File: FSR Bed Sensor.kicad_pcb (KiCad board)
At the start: 2 copper layers, 25.4 x 25.4 mm, 6 parts

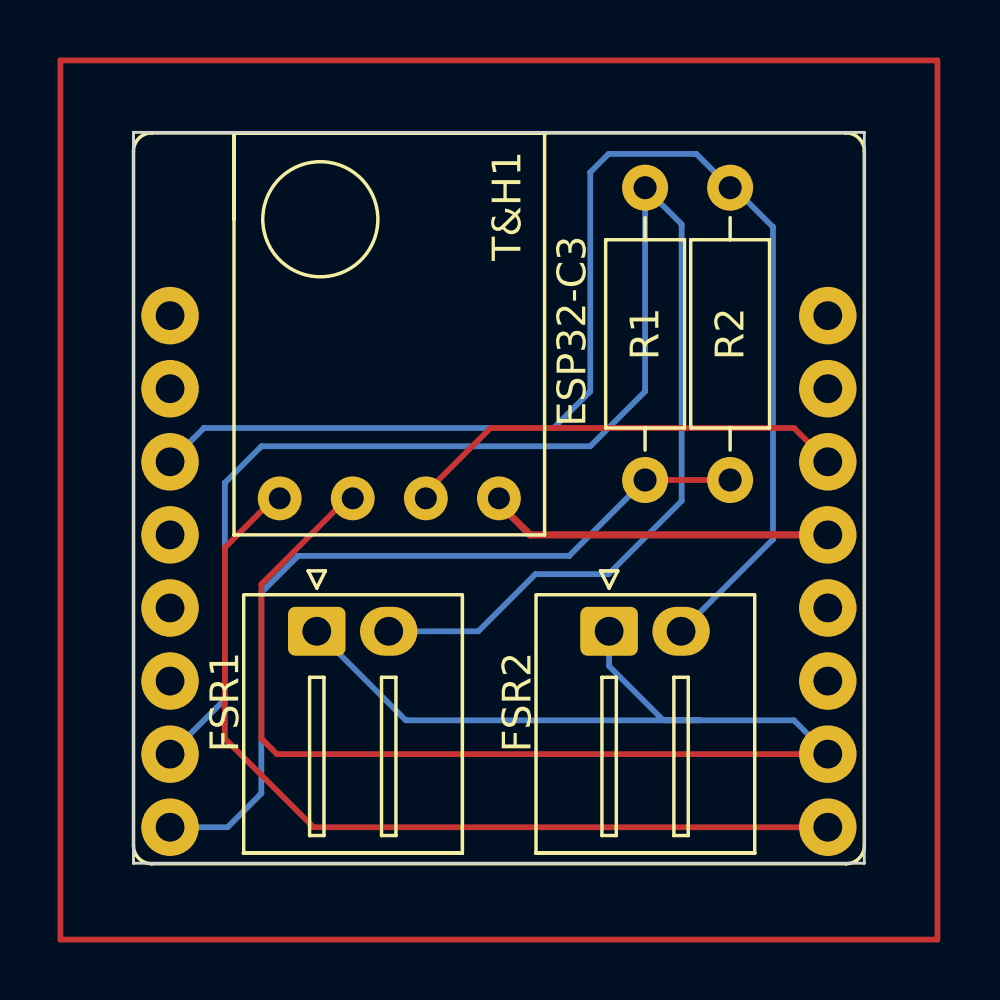
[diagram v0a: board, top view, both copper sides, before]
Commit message: Add files via upload
corrected the edge cut and added M2 mounting holes at the corners
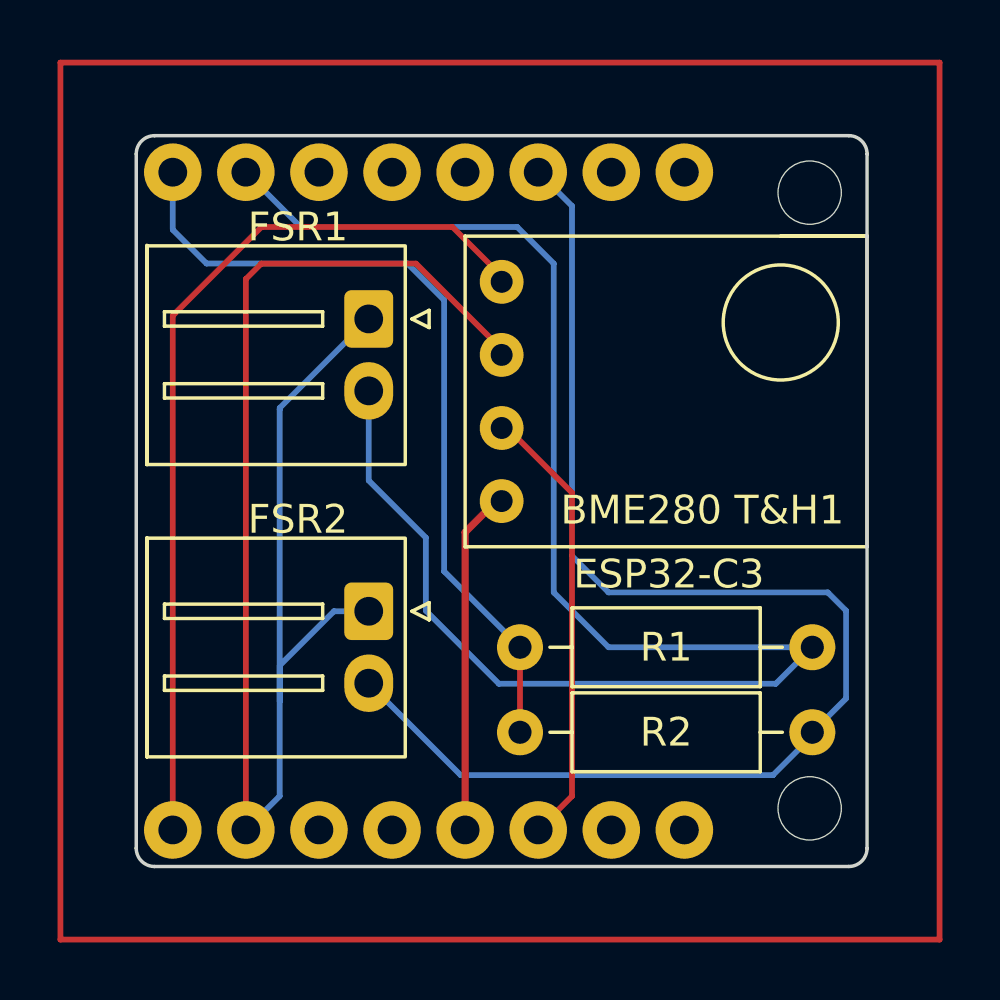
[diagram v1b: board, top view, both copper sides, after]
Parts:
- added REF**: MountingHole_2.2mm_M2, MountingHole:MountingHole_2.2mm_M2, F.Cu at (137.8, 136.6)
- added REF**: MountingHole_2.2mm_M2, MountingHole:MountingHole_2.2mm_M2, F.Cu at (137.8, 158.0)
- BME280 T&H1: renamed from T&H1
- moved FSR2 19.2 mm to (114.4, 152.4), turned to -90 degrees
- moved FSR1 19.2 mm to (114.4, 142.2), turned to -90 degrees
- moved ESP32-C3 17.8 mm to (114.4, 147.3), turned to -90 degrees
- moved R2 11.4 mm to (127.7, 155.4), turned to 0 degrees
- moved R1 7.26 mm to (127.7, 152.4), turned to 0 degrees
- moved BME280 T&H1 5.64 mm to (125.8, 143.5), turned to -90 degrees
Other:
- outline, holes or cut-outs redrawn
